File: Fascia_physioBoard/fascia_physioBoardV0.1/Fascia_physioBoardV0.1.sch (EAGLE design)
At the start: 88 parts, among them CN2 CA0612KRX7R9BB102, CN3 CA0612KRX7R9BB102, CN4 CA0612KRX7R9BB102, CN5 CA0612KRX7R9BB102, CN6 CA0612KRX7R9BB102, J1 MOLEX_52437-2471MOLEX_52437-2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, J2 MOLEX_52437-2471MOLEX_52437-2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, J3 MOLEX_51296-1294MOLEX_51296-1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, U1 ADS1299-X, U10 TPD4E1B06DCKR, U11 TPD4E1B06DCKR, U12 OPA320AIDBVRDBV5-L, U13 ADUM5028, U2 OPA2320AIDGKT_NOVA8-SOIC-L, U3 OPA2320AIDGKT_NOVAL8-SOIC-L, U4 HCNR200-300E, U5 OPA320AIDBVRDBV5-L, U6 TPD4E1B06DCKR, U7 TPD4E1B06DCKR, U8 TPD4E1B06DCKR, U9 TPD4E1B06DCKR

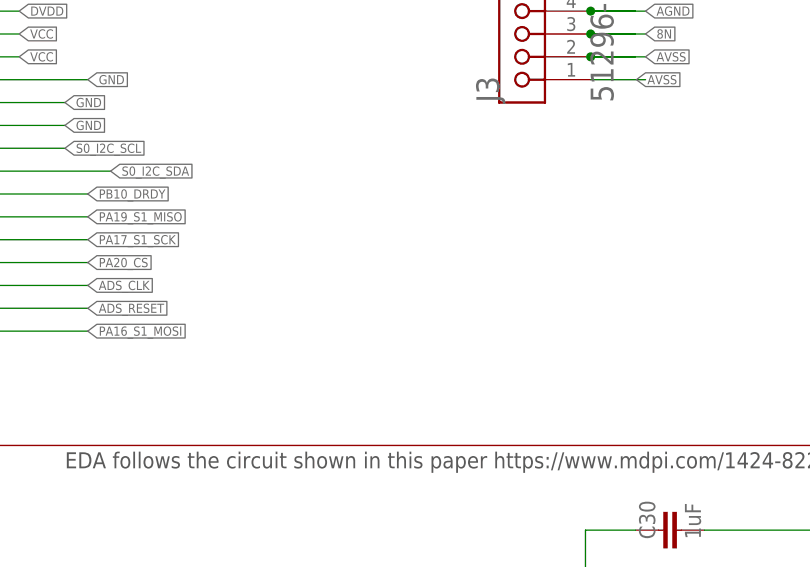
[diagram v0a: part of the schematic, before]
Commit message: Fixed SRB2 SRB1 issue
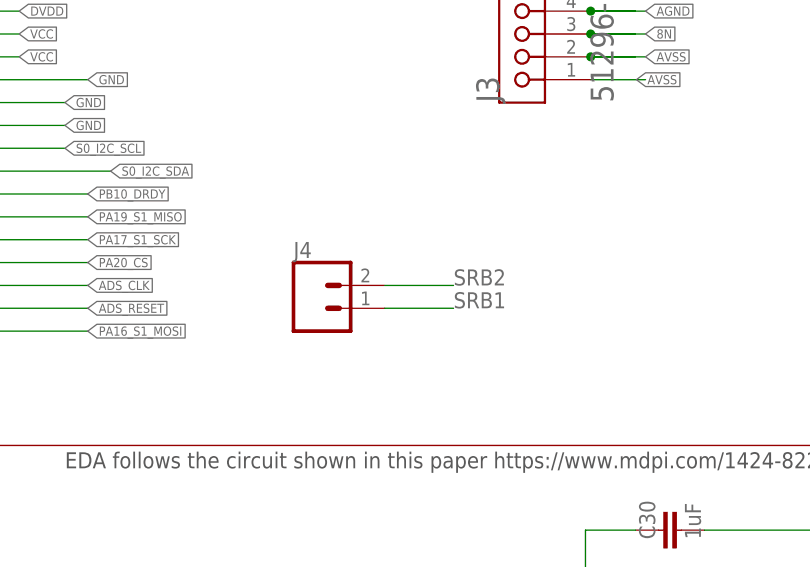
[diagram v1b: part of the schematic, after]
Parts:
- added J4: (no value), SparkFun-Connectors:CONN_02
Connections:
- net SRB1: now also J4.1
- net SRB2: now also J4.2
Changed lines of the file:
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@@
 <part name="GND36" library="SparkFun-PowerSymbols" library_urn="urn:adsk.eagle:library:530" deviceset="GND" device=""/>
 <part name="J3" library="Molex - 51296-1294" deviceset="MOLEX_51296-1294" device="MOLEX_51296-1294_0_0"/>
+<part name="J4" library="SparkFun-Connectors" library_urn="urn:adsk.eagle:library:513" deviceset="CONN_02" device="" package3d_urn="urn:adsk.eagle:package:38039/1"/>
 </parts>
 <sheets>
@@
 <instance part="J3" gate="G$0" x="213.36" y="162.56" smashed="yes" rot="R90">
 <attribute name="NAME" x="215.9" y="162.56" size="2.54" layer="95" rot="R90" align="top-left"/>
+</instance>
+<instance part="J4" gate="G$1" x="198.12" y="139.7" smashed="yes">
+<attribute name="VALUE" x="195.58" y="134.874" size="1.778" layer="96" font="vector"/>
+<attribute name="NAME" x="195.58" y="145.288" size="1.778" layer="95" font="vector"/>
 </instance>
 </instances>
@@
 <junction x="71.882" y="59.436"/>
 </segment>
+<segment>
+<pinref part="J4" gate="G$1" pin="1"/>
+<wire x1="205.74" y1="139.7" x2="213.36" y2="139.7" width="0.1524" layer="91"/>
+<label x="213.36" y="139.7" size="1.778" layer="95"/>
+</segment>
 </net>
 <net name="SRB2" class="0">
@@
 <pinref part="RN5" gate="G$1" pin="P$4"/>
 </segment>
-</net>
+<segment>
+<pinref part="J4" gate="G$1" pin="2"/>
+<wire x1="205.74" y1="142.24" x2="213.36" y2="142.24" width="0.1524" layer="91"/>
+<label x="213.36" y="142.24" size="1.778" layer="95"/>
+</segment>
+</net>

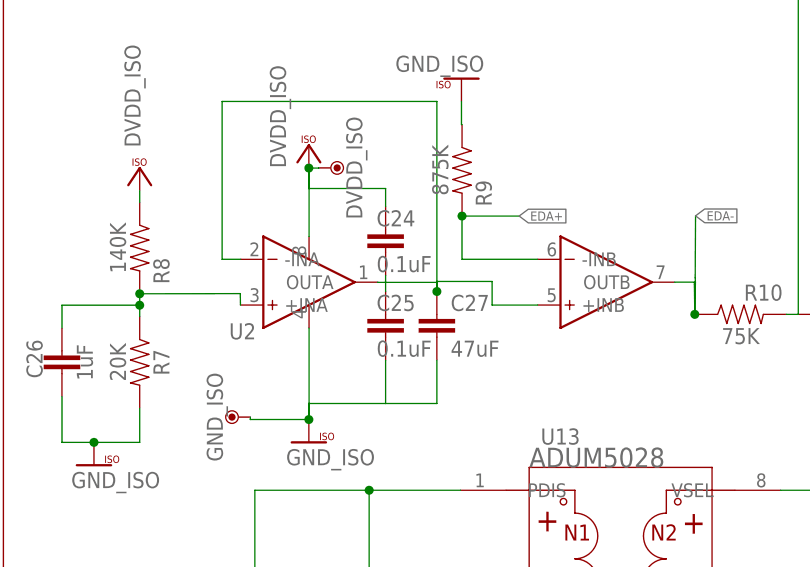
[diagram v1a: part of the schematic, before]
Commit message: fixed issues related to missing traces from pin 1 to the feedback to pin 2
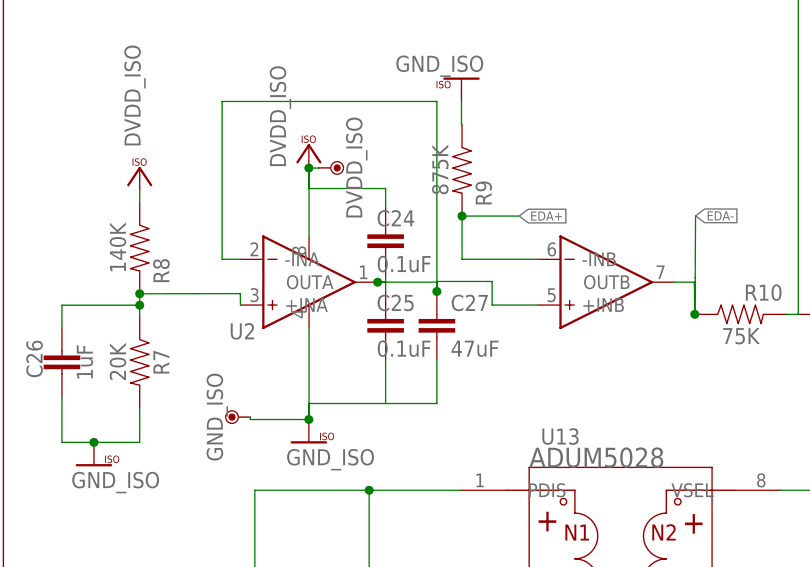
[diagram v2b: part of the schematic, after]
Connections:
- removed net N$12: C24.2, C25.1, C27.1, U2.+INB, U2.-INA
- new net N$8: C24.2, C25.1, C27.1, U2.+INB, U2.-INA, U2.OUTA
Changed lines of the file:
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@@
-</segment>
-</net>
-<net name="N$12" class="0">
-<segment>
-<pinref part="C24" gate="G$1" pin="2"/>
-<pinref part="C25" gate="G$1" pin="1"/>
-<wire x1="182.168" y1="74.662" x2="182.168" y2="73.9" width="0.1524" layer="91"/>
-<wire x1="182.168" y1="73.9" x2="182.168" y2="72.884" width="0.1524" layer="91"/>
-<wire x1="181.26" y1="73.9" x2="182.168" y2="73.9" width="0.1524" layer="91"/>
-<wire x1="182.168" y1="73.9" x2="187.864" y2="73.9" width="0.1524" layer="91"/>
-<pinref part="C27" gate="G$1" pin="1"/>
-<wire x1="187.864" y1="73.9" x2="187.864" y2="72.884" width="0.1524" layer="91"/>
-<wire x1="187.864" y1="72.884" x2="187.864" y2="94" width="0.1524" layer="91"/>
-<wire x1="187.864" y1="94" x2="164" y2="94" width="0.1524" layer="91"/>
-<junction x="187.864" y="72.884"/>
-<wire x1="164" y1="94" x2="164" y2="76.46" width="0.1524" layer="91"/>
-<pinref part="U2" gate="G$1" pin="-INA"/>
-<wire x1="164" y1="76.46" x2="166.04" y2="76.46" width="0.1524" layer="91"/>
-<pinref part="U2" gate="G$1" pin="+INB"/>
-<wire x1="199.06" y1="71.38" x2="194" y2="71.38" width="0.1524" layer="91"/>
-<wire x1="194" y1="71.38" x2="194" y2="74" width="0.1524" layer="91"/>
-<wire x1="194" y1="74" x2="187.864" y2="74" width="0.1524" layer="91"/>
-<wire x1="187.864" y1="74" x2="187.864" y2="72.884" width="0.1524" layer="91"/>
 </segment>
 </net>
@@
 </segment>
 </net>
+<net name="N$8" class="0">
+<segment>
+<pinref part="U2" gate="G$1" pin="OUTA"/>
+<pinref part="C24" gate="G$1" pin="2"/>
+<wire x1="182.168" y1="73.92" x2="182.168" y2="74.662" width="0.1524" layer="91"/>
+<pinref part="C25" gate="G$1" pin="1"/>
+<wire x1="182.168" y1="72.884" x2="182.168" y2="73.92" width="0.1524" layer="91"/>
+<wire x1="182.168" y1="73.92" x2="181.28" y2="73.92" width="0.1524" layer="91"/>
+<pinref part="C27" gate="G$1" pin="1"/>
+<wire x1="187.864" y1="73.9" x2="187.864" y2="72.884" width="0.1524" layer="91"/>
+<wire x1="187.864" y1="72.884" x2="187.864" y2="94" width="0.1524" layer="91"/>
+<wire x1="187.864" y1="94" x2="164" y2="94" width="0.1524" layer="91"/>
+<wire x1="164" y1="94" x2="164" y2="76.46" width="0.1524" layer="91"/>
+<pinref part="U2" gate="G$1" pin="-INA"/>
+<wire x1="164" y1="76.46" x2="166.04" y2="76.46" width="0.1524" layer="91"/>
+<pinref part="U2" gate="G$1" pin="+INB"/>
+<wire x1="199.06" y1="71.38" x2="194" y2="71.38" width="0.1524" layer="91"/>
+<wire x1="194" y1="71.38" x2="194" y2="74" width="0.1524" layer="91"/>
+<wire x1="194" y1="74" x2="187.864" y2="74" width="0.1524" layer="91"/>
+<wire x1="187.864" y1="74" x2="187.864" y2="72.884" width="0.1524" layer="91"/>
+<wire x1="181.28" y1="73.92" x2="187.864" y2="73.92" width="0.1524" layer="91"/>
+<wire x1="187.864" y1="73.92" x2="187.864" y2="72.884" width="0.1524" layer="91"/>
+<junction x="181.28" y="73.92"/>
+<junction x="187.864" y="72.884"/>
+</segment>
+</net>

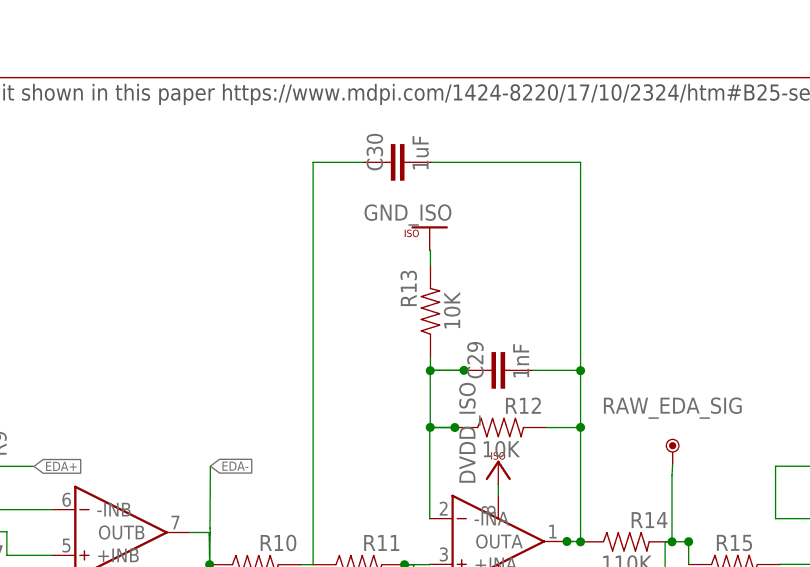
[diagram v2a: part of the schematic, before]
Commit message: removed wrong component
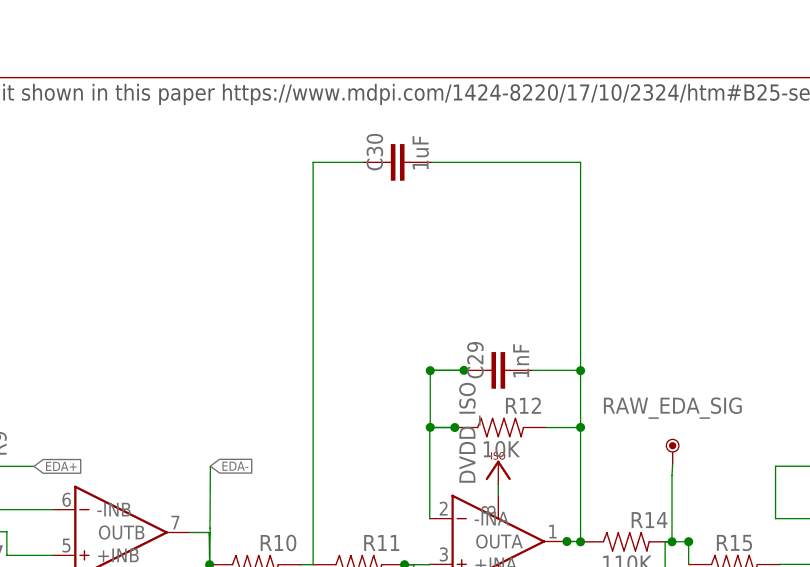
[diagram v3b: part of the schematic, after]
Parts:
- removed R13: 10K, novaXR:10K
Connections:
- net GND_ISO: no longer R13.2
- net N$10: no longer R13.1
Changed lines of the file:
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@@
 <?xml version="1.0" encoding="utf-8"?>
 <!DOCTYPE eagle SYSTEM "eagle.dtd">
-<eagle version="9.4.2">
+<eagle version="9.5.1">
 <drawing>
 <settings>
@@
 <part name="U$35" library="supply1" deviceset="GND_ISO" device=""/>
 <part name="R12" library="novaXR" deviceset="10K" device="" value="10K"/>
-<part name="R13" library="novaXR" deviceset="10K" device="" value="10K"/>
 <part name="R14" library="novaXR" deviceset="110K" device="" value="110K"/>
 <part name="C28" library="novaXR" deviceset="1UF" device="-0402T-16V-10%" value="1uF"/>
@@
 <part name="PA02_EDA_SIG" library="Arduino-utility" deviceset="TP" device="TP-0.8MM" value="DNP"/>
 <part name="GND_ISO" library="Arduino-utility" deviceset="TP" device="TP-0.8MM" value="DNP"/>
-<part name="U$9" library="supply1" deviceset="GND_ISO" device=""/>
 <part name="R15" library="novaXR" deviceset="150K" device="" value="150K"/>
 <part name="U4" library="HCNR200-300E" deviceset="HCNR200-300E" device=""/>
@@
 <attribute name="VALUE" x="248.85" y="84.06" size="1.778" layer="96" font="vector" align="top-center"/>
 </instance>
-<instance part="R13" gate="G$1" x="241.06" y="98.482" smashed="yes" rot="R90">
-<attribute name="NAME" x="239.536" y="101.022" size="1.778" layer="95" font="vector" rot="R90" align="bottom-center"/>
-<attribute name="VALUE" x="242.584" y="98.482" size="1.778" layer="96" font="vector" rot="R90" align="top-center"/>
-</instance>
 <instance part="R14" gate="G$1" x="262.82" y="72.884" smashed="yes">
 <attribute name="NAME" x="265.36" y="74.408" size="1.778" layer="95" font="vector" align="bottom-center"/>
@@
 <instance part="GND_ISO" gate="G$1" x="164.592" y="58.928" smashed="yes" rot="R90">
 <attribute name="NAME" x="164.084" y="58.928" size="1.778" layer="95" rot="R90" align="bottom-center"/>
-</instance>
-<instance part="U$9" gate="G$1" x="243.51" y="107.814" smashed="yes" rot="R180">
-<attribute name="VALUE" x="243.51" y="110.354" size="1.778" layer="96" rot="R180"/>
 </instance>
 <instance part="R15" gate="G$1" x="274.828" y="70.358" smashed="yes">
@@
 </segment>
 <segment>
-<pinref part="R13" gate="G$1" pin="2"/>
-<pinref part="U$9" gate="G$1" pin="GND_ISO"/>
-<wire x1="241.06" y1="103.562" x2="241.06" y2="105.274" width="0.1524" layer="91"/>
-<wire x1="241.06" y1="105.274" x2="240.97" y2="105.274" width="0.1524" layer="91"/>
-</segment>
-<segment>
 <pinref part="U3" gate="G$1" pin="V-"/>
 <pinref part="U$34" gate="G$1" pin="GND_ISO"/>
@@
 <wire x1="241.04" y1="91.9" x2="241.04" y2="91.934" width="0.1524" layer="91"/>
 <wire x1="241.04" y1="91.934" x2="244.786" y2="91.934" width="0.1524" layer="91"/>
-<pinref part="R13" gate="G$1" pin="1"/>
-<wire x1="241.06" y1="93.402" x2="241.06" y2="91.934" width="0.1524" layer="91"/>
 <wire x1="241.06" y1="91.934" x2="244.786" y2="91.934" width="0.1524" layer="91"/>
 <junction x="244.786" y="91.934"/>

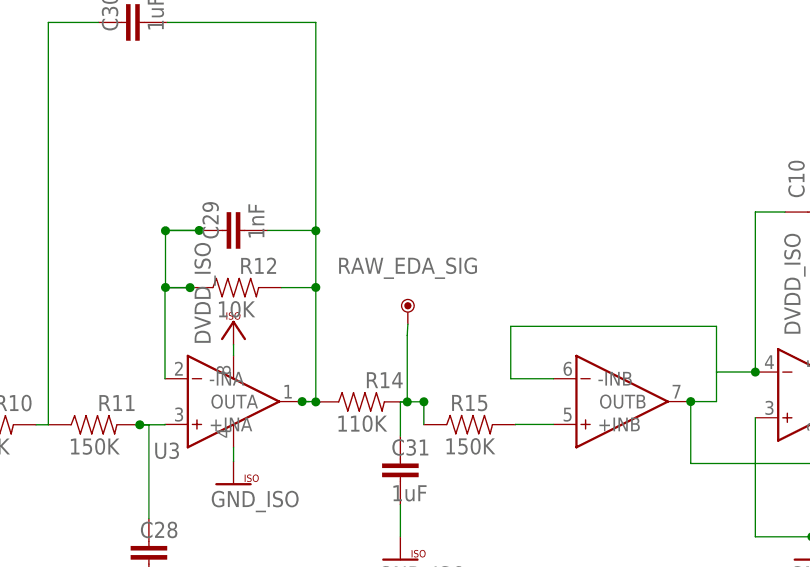
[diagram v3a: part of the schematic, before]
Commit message: changes to issue with R13
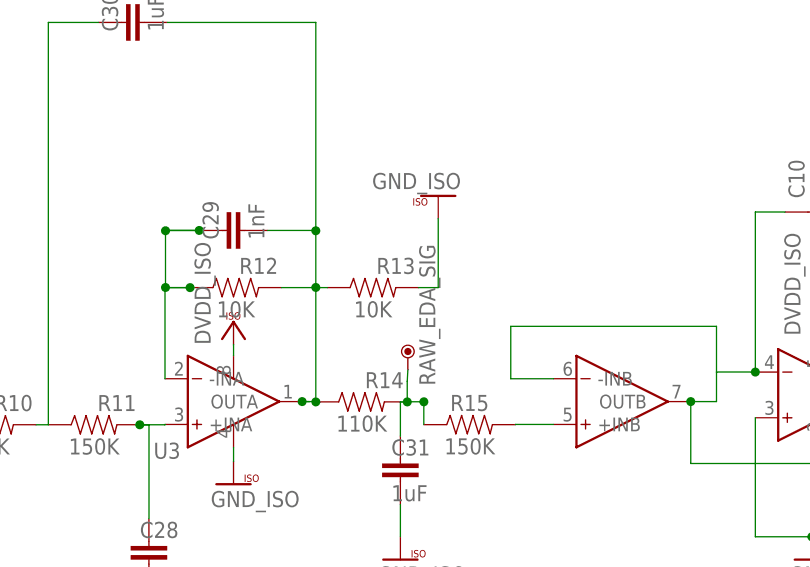
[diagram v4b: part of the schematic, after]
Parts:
- added R13: 10K, novaXR:10K
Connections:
- net GND_ISO: now also R13.2
- net N$11: now also R13.1
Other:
- moved on the sheet: RAW_EDA_SIG
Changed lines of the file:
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@@
 <part name="J3" library="Molex - 51296-1294" deviceset="MOLEX_51296-1294" device="MOLEX_51296-1294_0_0"/>
 <part name="J4" library="SparkFun-Connectors" library_urn="urn:adsk.eagle:library:513" deviceset="CONN_02" device="" package3d_urn="urn:adsk.eagle:package:38039/1"/>
+<part name="R13" library="novaXR" deviceset="10K" device="" value="10K"/>
+<part name="U$8" library="supply1" deviceset="GND_ISO" device=""/>
 </parts>
 <sheets>
@@
 <attribute name="NAME" x="177.8" y="86.614" size="1.778" layer="95" rot="R270" align="bottom-center"/>
 </instance>
-<instance part="RAW_EDA_SIG" gate="G$1" x="267.97" y="84.074" smashed="yes">
-<attribute name="NAME" x="267.97" y="87.122" size="1.778" layer="95" align="bottom-center"/>
+<instance part="RAW_EDA_SIG" gate="G$1" x="267.97" y="78.994" smashed="yes">
+<attribute name="NAME" x="271.018" y="82.55" size="1.778" layer="95" rot="R90" align="bottom-center"/>
 </instance>
 <instance part="PA02_EDA_SIG" gate="G$1" x="417.576" y="73.914" smashed="yes">
@@
 <attribute name="VALUE" x="195.58" y="134.874" size="1.778" layer="96" font="vector"/>
 <attribute name="NAME" x="195.58" y="145.288" size="1.778" layer="95" font="vector"/>
+</instance>
+<instance part="R13" gate="G$1" x="264.09" y="85.584" smashed="yes">
+<attribute name="NAME" x="266.63" y="87.108" size="1.778" layer="95" font="vector" align="bottom-center"/>
+<attribute name="VALUE" x="264.09" y="84.06" size="1.778" layer="96" font="vector" align="top-center"/>
+</instance>
+<instance part="U$8" gate="G$1" x="273.882" y="95.772" smashed="yes" rot="R180">
+<attribute name="VALUE" x="273.882" y="98.312" size="1.778" layer="96" rot="R180"/>
 </instance>
 </instances>
@@
 <label x="288.798" y="5.08" size="1.778" layer="95" xref="yes"/>
 </segment>
+<segment>
+<pinref part="U$8" gate="G$1" pin="GND_ISO"/>
+<pinref part="R13" gate="G$1" pin="2"/>
+<wire x1="271.342" y1="93.232" x2="271.342" y2="85.584" width="0.1524" layer="91"/>
+<wire x1="271.342" y1="85.584" x2="269.17" y2="85.584" width="0.1524" layer="91"/>
+</segment>
 </net>
 <net name="N$2" class="0">
@@
 <segment>
 <pinref part="RAW_EDA_SIG" gate="G$1" pin="P$1"/>
-<wire x1="267.9" y1="80.264" x2="267.97" y2="81.534" width="0.1524" layer="91"/>
+<wire x1="267.9" y1="75.184" x2="267.97" y2="76.454" width="0.1524" layer="91"/>
 <pinref part="C31" gate="G$1" pin="1"/>
 <wire x1="267.138" y1="72.884" x2="267.138" y2="69.09" width="0.1524" layer="91"/>
 <pinref part="R14" gate="G$1" pin="2"/>
 <wire x1="267.9" y1="72.884" x2="267.138" y2="72.884" width="0.1524" layer="91"/>
-<wire x1="267.9" y1="72.884" x2="267.9" y2="80.264" width="0.1524" layer="91"/>
+<wire x1="267.9" y1="72.884" x2="267.9" y2="75.184" width="0.1524" layer="91"/>
 <junction x="267.9" y="72.884"/>
 <pinref part="R15" gate="G$1" pin="1"/>
@@
 <junction x="257.74" y="85.6"/>
 </segment>
-</net>
+<segment>
+<pinref part="R13" gate="G$1" pin="1"/>
+<wire x1="259.01" y1="85.584" x2="257.81" y2="85.584" width="0.1524" layer="91"/>
+<wire x1="257.81" y1="85.584" x2="257.81" y2="85.598" width="0.1524" layer="91"/>
+</segment>
+</net>
